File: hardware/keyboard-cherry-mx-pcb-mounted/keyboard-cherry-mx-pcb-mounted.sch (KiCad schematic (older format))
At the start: 25 parts, among them J1 SWDConn, SW1 RST, U1 STM32F413RHTx, Y1 8MHz

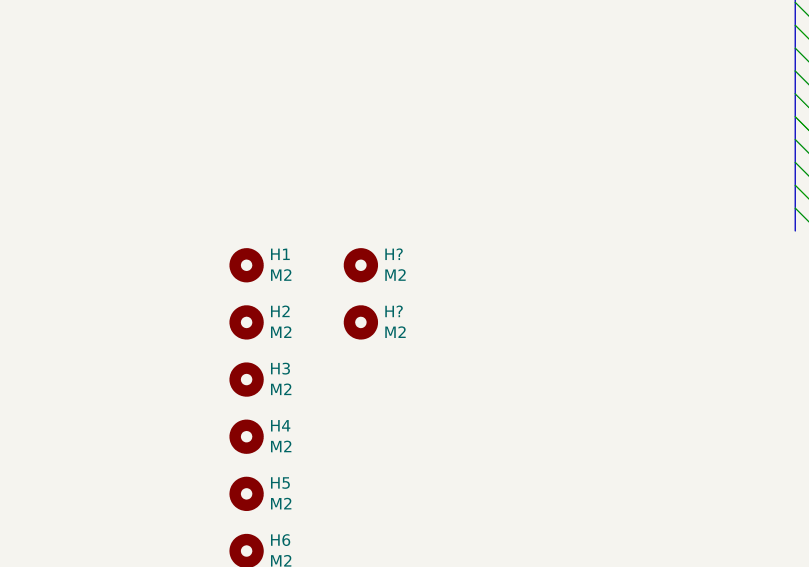
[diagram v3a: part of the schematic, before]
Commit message: Moves around bsp files to make firmware portable.
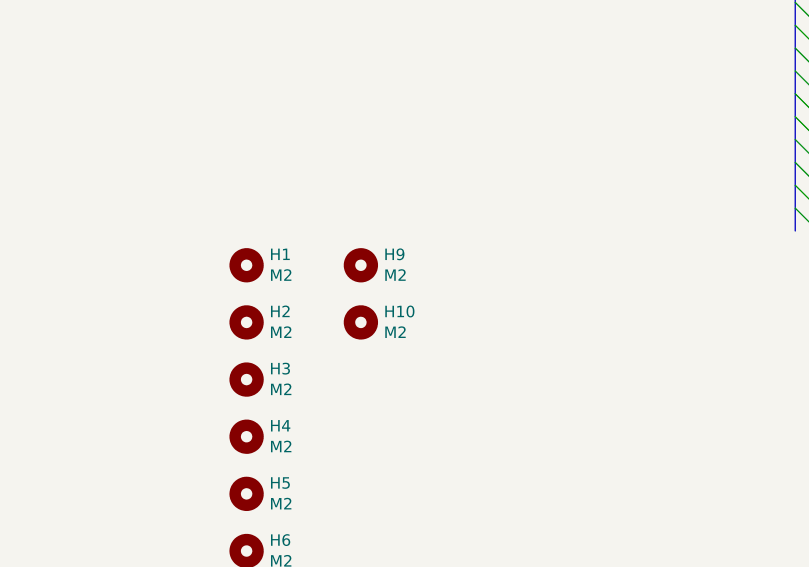
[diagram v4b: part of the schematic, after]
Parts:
- gave numbers to parts that had none: 2
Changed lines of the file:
@@
 $EndComp
 $Comp
-L Mechanical:MountingHole H?
+L Mechanical:MountingHole H9
 U 1 1 5E7549C0
 P 2500 5500
-F 0 "H?" H 2600 5546 50  0000 L CNN
+F 0 "H9" H 2600 5546 50  0000 L CNN
 F 1 "M2" H 2600 5455 50  0000 L CNN
 F 2 "MountingHole:MountingHole_2.2mm_M2" H 2500 5500 50  0001 C CNN
@@
 $EndComp
 $Comp
-L Mechanical:MountingHole H?
+L Mechanical:MountingHole H10
 U 1 1 5E7549C6
 P 2500 5750
-F 0 "H?" H 2600 5796 50  0000 L CNN
+F 0 "H10" H 2600 5796 50  0000 L CNN
 F 1 "M2" H 2600 5705 50  0000 L CNN
 F 2 "MountingHole:MountingHole_2.2mm_M2" H 2500 5750 50  0001 C CNN

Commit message: Adds P/N for crystal in cherry mx pcb mounted keyboard.
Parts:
- Y1: P/N (none) -> 7A-8.000MAAE-T
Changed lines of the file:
@@
 F 1 "8MHz" H 9250 2684 50  0000 C CNN
 F 2 "Crystal:Crystal_SMD_TXC_7A-2Pin_5x3.2mm" H 9250 2550 50  0001 C CNN
-F 3 "~" H 9250 2550 50  0001 C CNN
+F 3 "https://www.mouser.com/datasheet/2/417/7a-13881.pdf" H 9250 2550 50  0001 C CNN
+F 4 "7A-8.000MAAE-T" H 9250 2550 50  0001 C CNN "P/N"
 	1    9250 2550
 	1    0    0    -1
